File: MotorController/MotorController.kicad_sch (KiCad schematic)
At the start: 0 parts

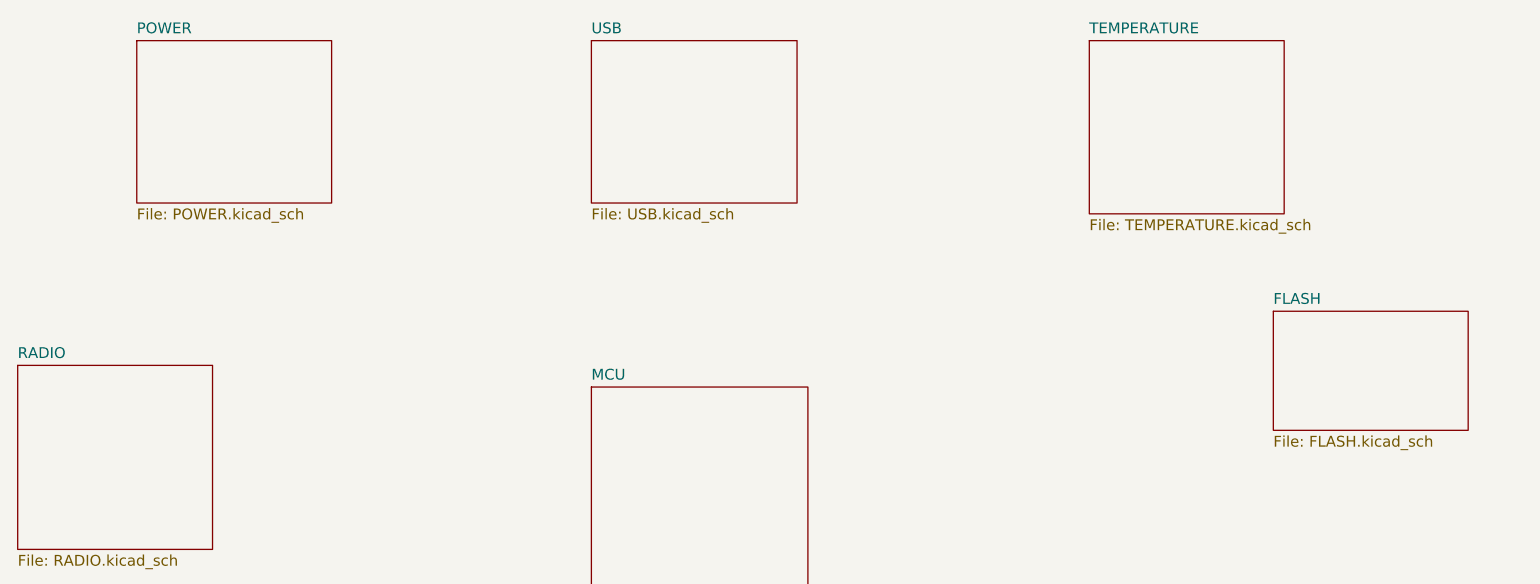
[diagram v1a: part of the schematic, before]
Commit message: Schematic Updates
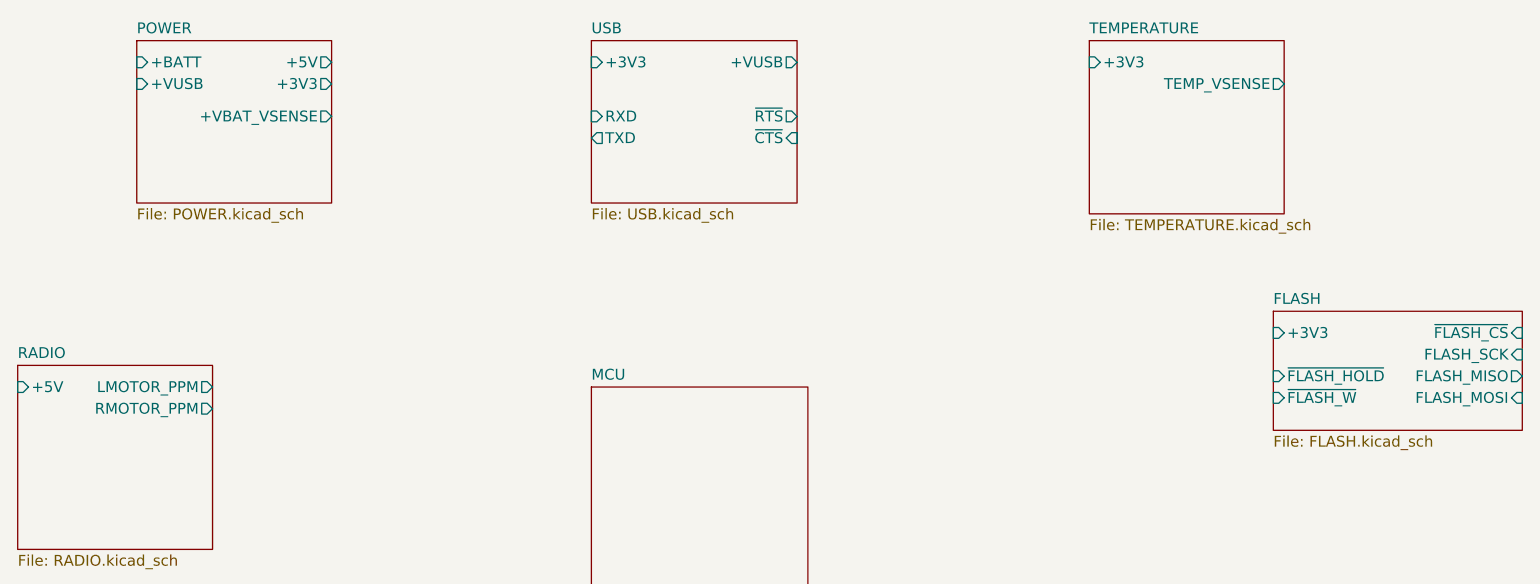
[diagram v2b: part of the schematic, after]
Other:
- sheet FLASH ports: added +3V3, FLASH_MISO, FLASH_MOSI, FLASH_SCK, ~{FLASH_CS}, ~{FLASH_HOLD}, ~{FLASH_W}; removed none
- sheet POWER ports: added +3V3, +5V, +BATT, +VBAT_VSENSE, +VUSB; removed none
- sheet RADIO ports: added +5V, LMOTOR_PPM, RMOTOR_PPM; removed none
- sheet TEMPERATURE ports: added +3V3, TEMP_VSENSE; removed none
- sheet USB ports: added +3V3, +VUSB, RXD, TXD, ~{CTS}, ~{RTS}; removed none

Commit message: Updates
Updates
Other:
- sheet LMOTOR ports: added +3V3, +5V, +BATT, LMOTOR_BACKWARDS, LMOTOR_FORWARD; removed none
- sheet MCU ports: added +3V3, FLASH_MISO, FLASH_MOSI, FLASH_SCK, RXD, TXD, ~{FLASH_CS}; removed none
- sheet RMOTOR ports: added +3V3, +5V, +BATT, RMOTOR_BACKWARDS, RMOTOR_FORWARD; removed none

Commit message: More updates
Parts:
- added J? (x2): Conn_01x02, symbol Connector_Generic:Conn_01x02
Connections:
- net POWER/+BATT: now also J?.1 (Pin_1)
- new net +XT_VBAT: J?.1 (Pin_1)
- new net GND: J?.2 (Pin_2), J?.2 (Pin_2)
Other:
- sheet MCU ports: added +MOTOR_ISENSE, +TEMP_VSENSE, +VBAT_VSENSE, +XT_ISENSE, LMOTOR_BACKWARD, LMOTOR_FORWARD, LMOTOR_PPM, RMOTOR_BACKWARD, RMOTOR_FORWARD, RMOTOR_PPM; removed none
- sheet POWER ports: added +MOTOR_VBAT, +XT_VBAT, MOTOR_ISENSE, XT_ISENSE; removed none
- note added: "CHECK USB TO UART PINS"

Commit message: Updates
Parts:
- added J3: Conn_01x03, Connector_PinHeader_2.54mm:PinHeader_1x03_P2.54mm_Vertical, symbol Connector_Generic:Conn_01x03
- J1, J2: renamed from J?; footprint (none) -> Connector_PinHeader_2.54mm:PinHeader_1x02_P2.54mm_Vertical
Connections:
- net GND: now also J3.3 (Pin_3)
- new net MCU/SWCLK: J3.1 (Pin_1)
- new net MCU/SWDIO: J3.2 (Pin_2)
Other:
- sheet MCU ports: added SWCLK, SWDIO; removed none
- note removed: "CHECK USB TO UART PINS"

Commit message: So many updates
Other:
- sheet MCU ports: added +LMOTOR_ISENSE, +LTEMP_VSENSE, +RMOTOR_ISENSE, +RTEMP_VSENSE; removed +MOTOR_ISENSE, +TEMP_VSENSE
- sheet POWER ports: added +LMOTOR_VBAT, +RMOTOR_VBAT, LMOTOR_ISENSE, RMOTOR_ISENSE; removed +MOTOR_VBAT, MOTOR_ISENSE
- sheet TEMPERATURE ports: added LTEMP_VSENSE, RTEMP_VSENSE; removed TEMP_VSENSE
